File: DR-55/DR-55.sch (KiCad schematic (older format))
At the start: 0 parts

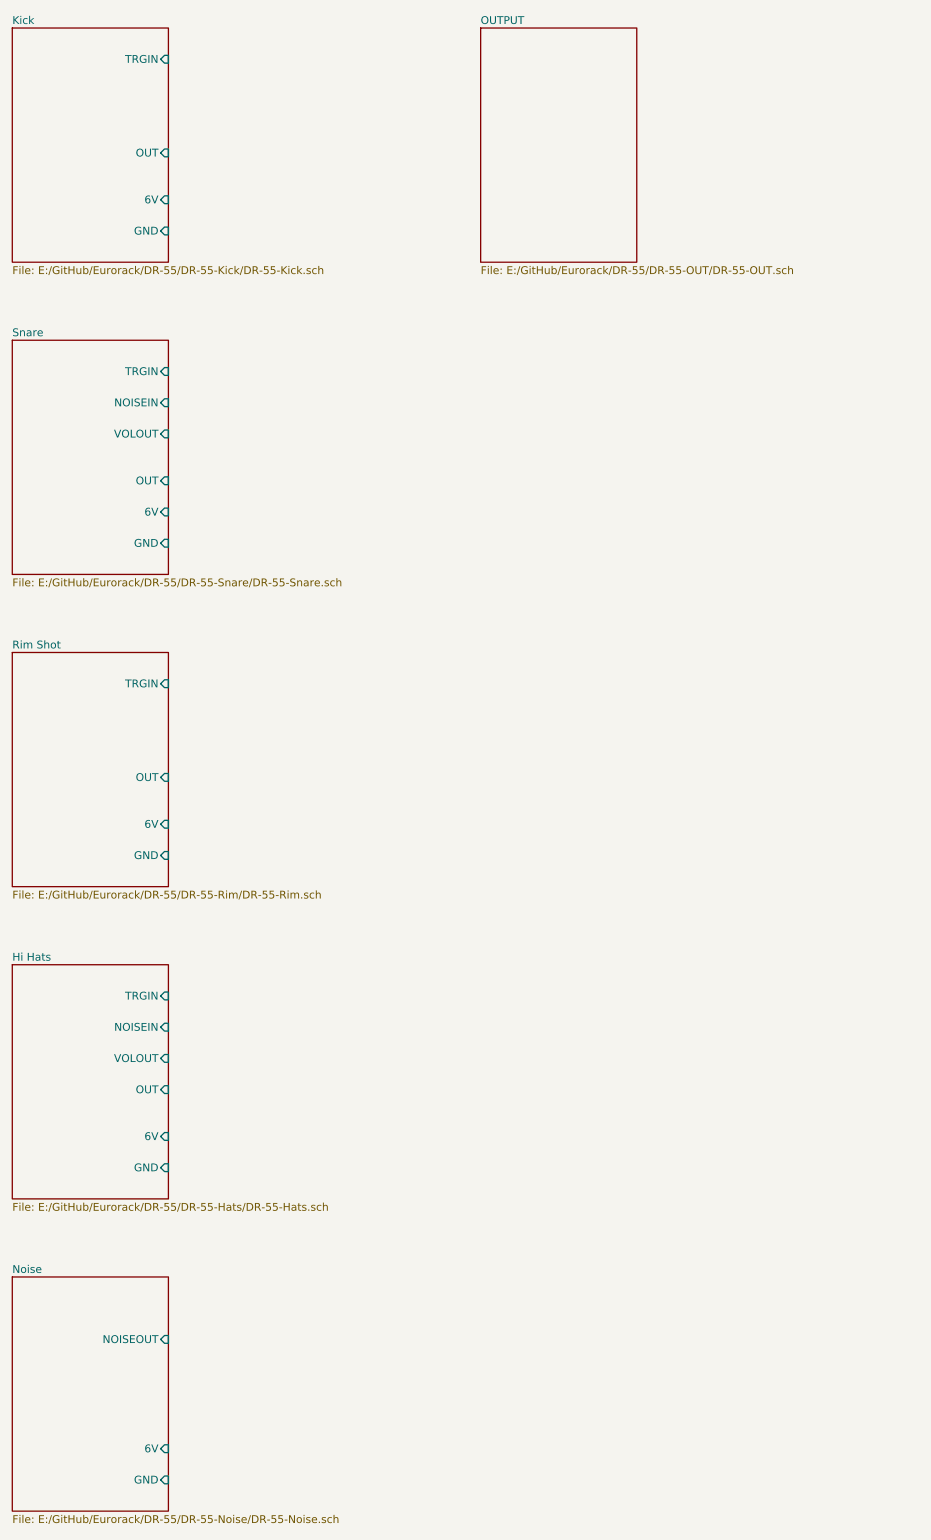
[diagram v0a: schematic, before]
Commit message: Output finished
Finished the output schematic and routed alll the traces between the submodules
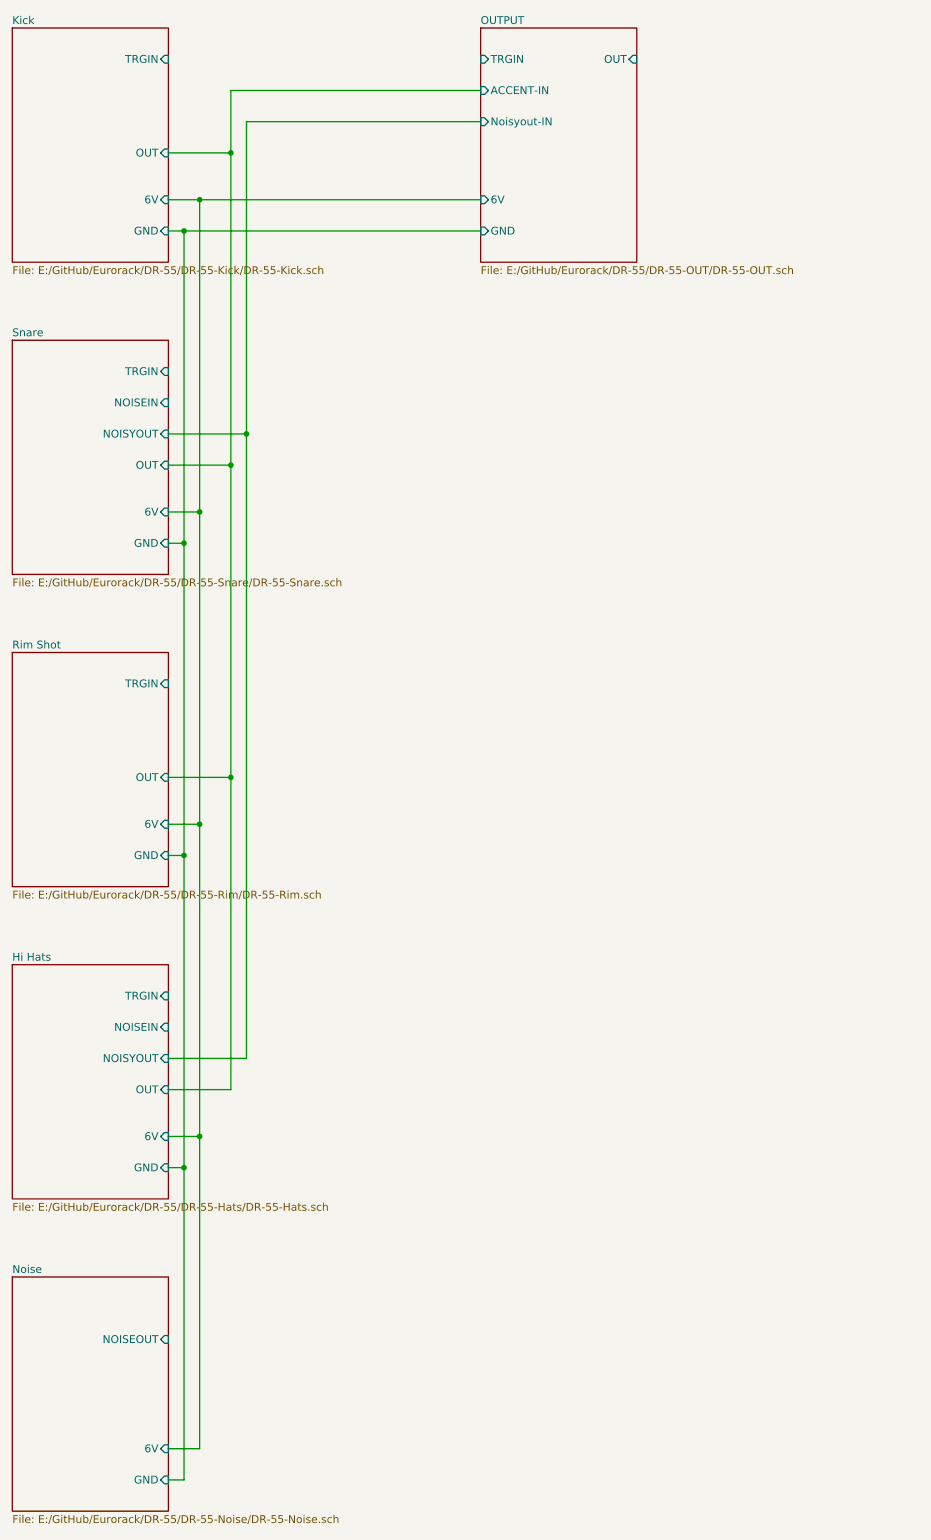
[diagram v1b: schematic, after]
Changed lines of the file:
@@
 F2 "TRGIN" I R 2000 3200 50
 F3 "GND" I R 2000 4300 50
-F4 "OUT" I R 2000 3900 50
+F4 "OUT" I R 2000 3800 50
 F5 "6V" I R 2000 4100 50
-F6 "VOLOUT" I R 2000 3600 50
-F7 "NOISEIN" I R 2000 3400 50
+F6 "NOISEIN" I R 2000 3400 50
+F7 "NOISYOUT" I R 2000 3600 50
 $EndSheet
 $Sheet
@@
 F4 "NOISEIN" I R 2000 7400 50
 F5 "OUT" I R 2000 7800 50
-F6 "VOLOUT" I R 2000 7600 50
-F7 "6V" I R 2000 8100 50
+F6 "6V" I R 2000 8100 50
+F7 "NOISYOUT" I R 2000 7600 50
 $EndSheet
 $Sheet
@@
 F0 "OUTPUT" 50
 F1 "E:/GitHub/Eurorack/DR-55/DR-55-OUT/DR-55-OUT.sch" 50
+F2 "TRGIN" I L 4000 1200 50
+F3 "GND" I L 4000 2300 50
+F4 "OUT" I R 5000 1200 50
+F5 "6V" I L 4000 2100 50
+F6 "ACCENT-IN" I L 4000 1400 50
+F7 "Noisyout-IN" I L 4000 1600 50
 $EndSheet
 $Sheet
@@
 F5 "GND" I R 2000 2300 50
 $EndSheet
+Wire Wire Line
+	4000 2100 2200 2100
+Wire Wire Line
+	4000 2300 2100 2300
+Wire Wire Line
+	2100 2300 2100 4300
+Wire Wire Line
+	2100 4300 2000 4300
+Connection ~ 2100 2300
+Wire Wire Line
+	2100 2300 2000 2300
+Wire Wire Line
+	2100 4300 2100 6300
+Wire Wire Line
+	2100 6300 2000 6300
+Connection ~ 2100 4300
+Wire Wire Line
+	2100 6300 2100 8300
+Wire Wire Line
+	2100 8300 2000 8300
+Connection ~ 2100 6300
+Wire Wire Line
+	2100 8300 2100 10300
+Wire Wire Line
+	2100 10300 2000 10300
+Connection ~ 2100 8300
+Connection ~ 2200 2100
+Wire Wire Line
+	2200 2100 2000 2100
+Wire Wire Line
+	2200 10100 2000 10100
+Wire Wire Line
+	2000 8100 2200 8100
+Connection ~ 2200 8100
+Wire Wire Line
+	2200 8100 2200 10100
+Wire Wire Line
+	2000 6100 2200 6100
+Connection ~ 2200 6100
+Wire Wire Line
+	2200 6100 2200 8100
+Wire Wire Line
+	2000 4100 2200 4100
+Connection ~ 2200 4100
+Wire Wire Line
+	2200 4100 2200 6100
+Wire Wire Line
+	2200 2100 2200 4100
+Wire Wire Line
+	2000 1800 2400 1800
+Wire Wire Line
+	2400 1800 2400 1400
+Wire Wire Line
+	2400 1400 4000 1400
+Wire Wire Line
+	2400 1800 2400 3800
+Wire Wire Line
+	2400 7800 2000 7800
+Connection ~ 2400 1800
+Wire Wire Line
+	2000 5800 2400 5800
+Connection ~ 2400 5800
+Wire Wire Line
+	2400 5800 2400 7800
+Wire Wire Line
+	2000 3800 2400 3800
+Connection ~ 2400 3800
+Wire Wire Line
+	2400 3800 2400 5800
+Wire Wire Line
+	4000 1600 2500 1600
+Wire Wire Line
+	2500 1600 2500 3600
+Wire Wire Line
+	2500 7600 2000 7600
+Wire Wire Line
+	2000 3600 2500 3600
+Connection ~ 2500 3600
+Wire Wire Line
+	2500 3600 2500 7600
 $EndSCHEMATC

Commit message: small changes
just some small overall changes (not relevant
)
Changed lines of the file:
@@
 $EndDescr
-$Sheet
-S 1000 3000 1000 1500
-U 62740CD0
-F0 "Snare" 50
-F1 "E:/GitHub/Eurorack/DR-55/DR-55-Snare/DR-55-Snare.sch" 50
-F2 "TRGIN" I R 2000 3200 50
-F3 "GND" I R 2000 4300 50
-F4 "OUT" I R 2000 3800 50
-F5 "6V" I R 2000 4100 50
-F6 "NOISEIN" I R 2000 3400 50
-F7 "NOISYOUT" I R 2000 3600 50
-$EndSheet
 $Sheet
 S 1000 7000 1000 1500
@@
 F5 "GND" I R 2000 2300 50
 $EndSheet
-Wire Wire Line
-	4000 2100 2200 2100
-Wire Wire Line
-	4000 2300 2100 2300
 Wire Wire Line
 	2100 2300 2100 4300
@@
 Wire Wire Line
 	2500 3600 2500 7600
+$Comp
+L power:+6V #PWR?
+U 1 1 62887F3E
+P 3900 2100
+AR Path="/6276643A/62887F3E" Ref="#PWR?"  Part="1"
+AR Path="/62740CD0/62887F3E" Ref="#PWR?"  Part="1"
+AR Path="/62804339/62887F3E" Ref="#PWR?"  Part="1"
+AR Path="/627A1DA3/62887F3E" Ref="#PWR?"  Part="1"
+AR Path="/62887F3E" Ref="#PWR?"  Part="1"
+F 0 "#PWR?" H 3900 1950 50  0001 C CNN
+F 1 "+6V" H 3915 2273 50  0000 C CNN
+F 2 "" H 3900 2100 50  0001 C CNN
+F 3 "" H 3900 2100 50  0001 C CNN
+	1    3900 2100
+	1    0    0    -1
+$EndComp
+$Comp
+L power:GND #PWR?
+U 1 1 6288900A
+P 3900 2300
+AR Path="/6276643A/6288900A" Ref="#PWR?"  Part="1"
+AR Path="/62740CD0/6288900A" Ref="#PWR?"  Part="1"
+AR Path="/62804339/6288900A" Ref="#PWR?"  Part="1"
+AR Path="/627A1DA3/6288900A" Ref="#PWR?"  Part="1"
+F 0 "#PWR?" H 3900 2050 50  0001 C CNN
+F 1 "GND" H 3905 2127 50  0000 C CNN
+F 2 "" H 3900 2300 50  0001 C CNN
+F 3 "" H 3900 2300 50  0001 C CNN
+	1    3900 2300
+	1    0    0    -1
+$EndComp
+Wire Wire Line
+	2100 2300 3900 2300
+Connection ~ 3900 2300
+Wire Wire Line
+	3900 2300 4000 2300
+Wire Wire Line
+	2200 2100 3900 2100
+Connection ~ 3900 2100
+Wire Wire Line
+	3900 2100 4000 2100
+$Sheet
+S 1000 3000 1000 1500
+U 62740CD0
+F0 "Snare" 50
+F1 "E:/GitHub/Eurorack/DR-55/DR-55-Snare/DR-55-Snare.sch" 50
+F2 "TRGIN" I R 2000 3200 50
+F3 "GND" I R 2000 4300 50
+F4 "OUT" I R 2000 3800 50
+F5 "6V" I R 2000 4100 50
+F6 "NOISEIN" I R 2000 3400 50
+F7 "NOISYOUT" I R 2000 3600 50
+$EndSheet
+Wire Wire Line
+	2000 3400 2700 3400
+Wire Wire Line
+	2700 3400 2700 7400
+Wire Wire Line
+	2700 7400 2000 7400
+Wire Wire Line
+	2700 7400 2700 9400
+Wire Wire Line
+	2700 9400 2000 9400
+Connection ~ 2700 7400
 $EndSCHEMATC

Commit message: Values
Added Values to all components
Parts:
- added J?: OUT, symbol Eurorack:Thonkiconn
- added J?: KICK, symbol Eurorack:Thonkiconn
- added J?: SNARE, symbol Eurorack:Thonkiconn
- added J?: RIM, symbol Eurorack:Thonkiconn
- added J?: HIHAT, symbol Eurorack:Thonkiconn
- added J?: ACCENT, symbol Eurorack:Thonkiconn
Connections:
- net GND: now also J?.3, J?.3, J?.3, J?.3, J?.3, J?.3
- net Hi Hats/TRGIN: now also J?.1
- net Kick/TRGIN: now also J?.1
- net OUTPUT/OUT: now also J?.1
- net OUTPUT/TRGIN: now also J?.1
- net Rim Shot/TRGIN: now also J?.1
- net Snare/TRGIN: now also J?.1
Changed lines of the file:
@@
-$EndSheet
-$Sheet
-S 4000 1000 1000 1500
-U 627A1DA3
-F0 "OUTPUT" 50
-F1 "E:/GitHub/Eurorack/DR-55/DR-55-OUT/DR-55-OUT.sch" 50
-F2 "TRGIN" I L 4000 1200 50
-F3 "GND" I L 4000 2300 50
-F4 "OUT" I R 5000 1200 50
-F5 "6V" I L 4000 2100 50
-F6 "ACCENT-IN" I L 4000 1400 50
-F7 "Noisyout-IN" I L 4000 1600 50
 $EndSheet
 $Sheet
@@
 AR Path="/62804339/6288900A" Ref="#PWR?"  Part="1"
 AR Path="/627A1DA3/6288900A" Ref="#PWR?"  Part="1"
+AR Path="/6288900A" Ref="#PWR?"  Part="1"
 F 0 "#PWR?" H 3900 2050 50  0001 C CNN
 F 1 "GND" H 3905 2127 50  0000 C CNN
@@
 $EndComp
 Wire Wire Line
-	2100 2300 3900 2300
+	2100 2300 3500 2300
 Connection ~ 3900 2300
 Wire Wire Line
@@
 	2700 9400 2000 9400
 Connection ~ 2700 7400
+$Comp
+L Eurorack:Thonkiconn J?
+U 1 1 627AD8C4
+P 5750 1200
+F 0 "J?" H 5794 1168 50  0000 L CNN
+F 1 "OUT" H 5794 1077 50  0000 L CNN
+F 2 "" H 5650 1250 50  0001 C CNN
+F 3 "" H 5650 1250 50  0001 C CNN
+	1    5750 1200
+	1    0    0    -1
+$EndComp
+$Sheet
+S 4000 1000 1000 1500
+U 627A1DA3
+F0 "OUTPUT" 50
+F1 "E:/GitHub/Eurorack/DR-55/DR-55-OUT/DR-55-OUT.sch" 50
+F2 "TRGIN" I L 4000 1200 50
+F3 "GND" I L 4000 2300 50
+F4 "OUT" I R 5000 1200 50
+F5 "6V" I L 4000 2100 50
+F6 "ACCENT-IN" I L 4000 1400 50
+F7 "Noisyout-IN" I L 4000 1600 50
+$EndSheet
+Wire Wire Line
+	5000 1200 5500 1200
+$Comp
+L power:GND #PWR?
+U 1 1 627B2033
+P 5750 1500
+AR Path="/6276643A/627B2033" Ref="#PWR?"  Part="1"
+AR Path="/62740CD0/627B2033" Ref="#PWR?"  Part="1"
+AR Path="/62804339/627B2033" Ref="#PWR?"  Part="1"
+AR Path="/627A1DA3/627B2033" Ref="#PWR?"  Part="1"
+AR Path="/627B2033" Ref="#PWR?"  Part="1"
+F 0 "#PWR?" H 5750 1250 50  0001 C CNN
+F 1 "GND" H 5755 1327 50  0000 C CNN
+F 2 "" H 5750 1500 50  0001 C CNN
+F 3 "" H 5750 1500 50  0001 C CNN
+	1    5750 1500
+	1    0    0    -1
+$EndComp
+Wire Wire Line
+	5750 1500 5750 1400
+$Comp
+L Eurorack:Thonkiconn J?
+U 1 1 627B3297
+P 4250 3000
+F 0 "J?" H 4294 2968 50  0000 L CNN
+F 1 "KICK" H 4294 2877 50  0000 L CNN
+F 2 "" H 4150 3050 50  0001 C CNN
+F 3 "" H 4150 3050 50  0001 C CNN
+	1    4250 3000
+	1    0    0    -1
+$EndComp
+$Comp
+L Eurorack:Thonkiconn J?
+U 1 1 627B659A
+P 4250 3500
+F 0 "J?" H 4294 3468 50  0000 L CNN
+F 1 "SNARE" H 4294 3377 50  0000 L CNN
+F 2 "" H 4150 3550 50  0001 C CNN
+F 3 "" H 4150 3550 50  0001 C CNN
+	1    4250 3500
+	1    0    0    -1
+$EndComp
+$Comp
+L Eurorack:Thonkiconn J?
+U 1 1 627B6F00
+P 4250 4000
+F 0 "J?" H 4294 3968 50  0000 L CNN
+F 1 "RIM" H 4294 3877 50  0000 L CNN
+F 2 "" H 4150 4050 50  0001 C CNN
+F 3 "" H 4150 4050 50  0001 C CNN
+	1    4250 4000
+	1    0    0    -1
+$EndComp
+$Comp
+L Eurorack:Thonkiconn J?
+U 1 1 627B7907
+P 4250 4500
+F 0 "J?" H 4294 4468 50  0000 L CNN
+F 1 "HIHAT" H 4294 4377 50  0000 L CNN
+F 2 "" H 4150 4550 50  0001 C CNN
+F 3 "" H 4150 4550 50  0001 C CNN
+	1    4250 4500
+	1    0    0    -1
+$EndComp
+$Comp
+L Eurorack:Thonkiconn J?
+U 1 1 627B86EE
+P 4250 5000
+F 0 "J?" H 4294 4968 50  0000 L CNN
+F 1 "ACCENT" H 4294 4877 50  0000 L CNN
+F 2 "" H 4150 5050 50  0001 C CNN
+F 3 "" H 4150 5050 50  0001 C CNN
+	1    4250 5000
+	1    0    0    -1
+$EndComp
+Wire Wire Line
+	4250 3200 3500 3200
+Wire Wire Line
+	3500 3200 3500 3700
+Wire Wire Line
+	3500 5200 4250 5200
+Wire Wire Line
+	4250 4700 3500 4700
+Connection ~ 3500 4700
+Wire Wire Line
+	3500 4700 3500 5200
+Wire Wire Line
+	3500 4200 4250 4200
+Connection ~ 3500 4200
+Wire Wire Line
+	3500 4200 3500 4700
+Wire Wire Line
+	4250 3700 3500 3700
+Connection ~ 3500 3700
+Wire Wire Line
+	3500 3700 3500 4200
+Wire Wire Line
+	3500 3200 3500 2300
+Connection ~ 3500 3200
+Connection ~ 3500 2300
+Wire Wire Line
+	3500 2300 3900 2300
+Wire Wire Line
+	4000 3000 2700 3000
+Wire Wire Line
+	2700 3000 2700 1200
+Wire Wire Line
+	4000 3500 2800 3500
+Wire Wire Line
+	2800 3500 2800 3200
+Wire Wire Line
+	2800 3200 2000 3200
+Wire Wire Line
+	4000 4000 2900 4000
+Wire Wire Line
+	2900 4000 2900 5200
+Wire Wire Line
+	2900 5200 2000 5200
+Wire Wire Line
+	4000 4500 3000 4500
+Wire Wire Line
+	3000 4500 3000 7200
+Wire Wire Line
+	3000 7200 2000 7200
+Wire Wire Line
+	4000 5000 3100 5000
+Wire Wire Line
+	3100 5000 3100 1200
+Wire Wire Line
+	3100 1200 4000 1200
+Wire Wire Line
+	2700 1200 2000 1200
 $EndSCHEMATC

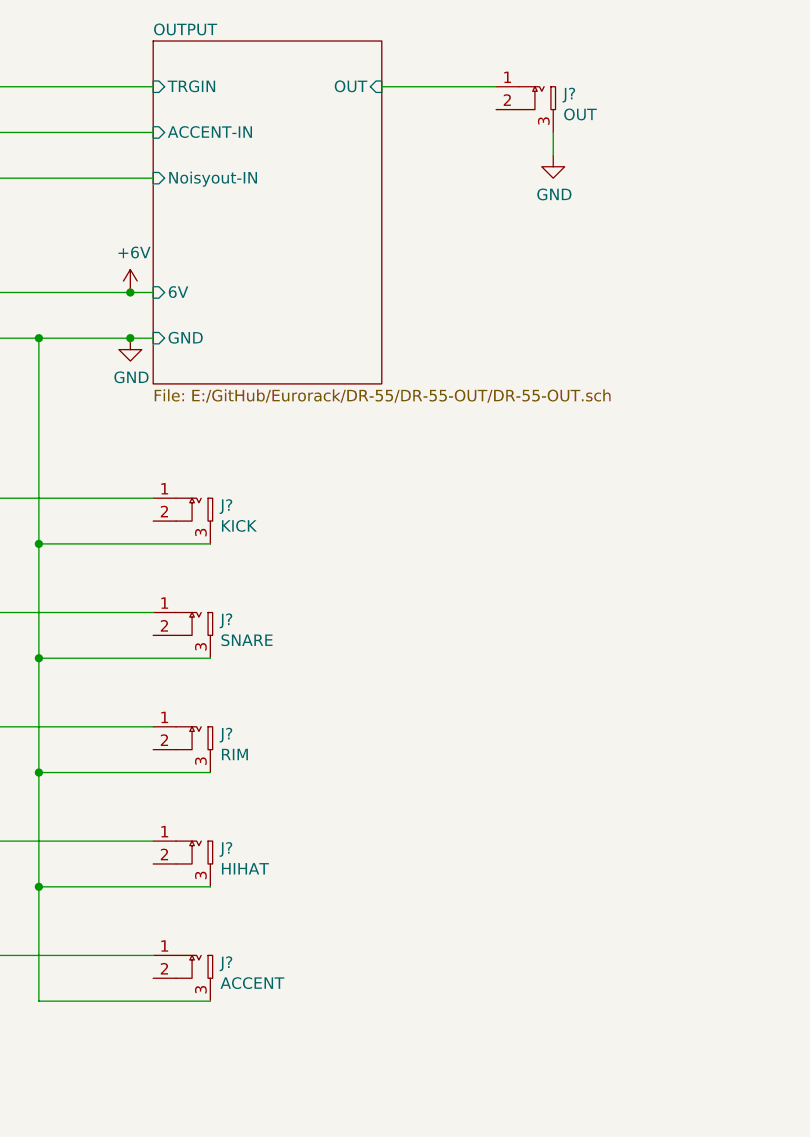
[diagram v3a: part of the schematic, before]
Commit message: Footprints added
Added most of the footprints for a 0805 SMD PCB. some placeholder footprints added and some missing
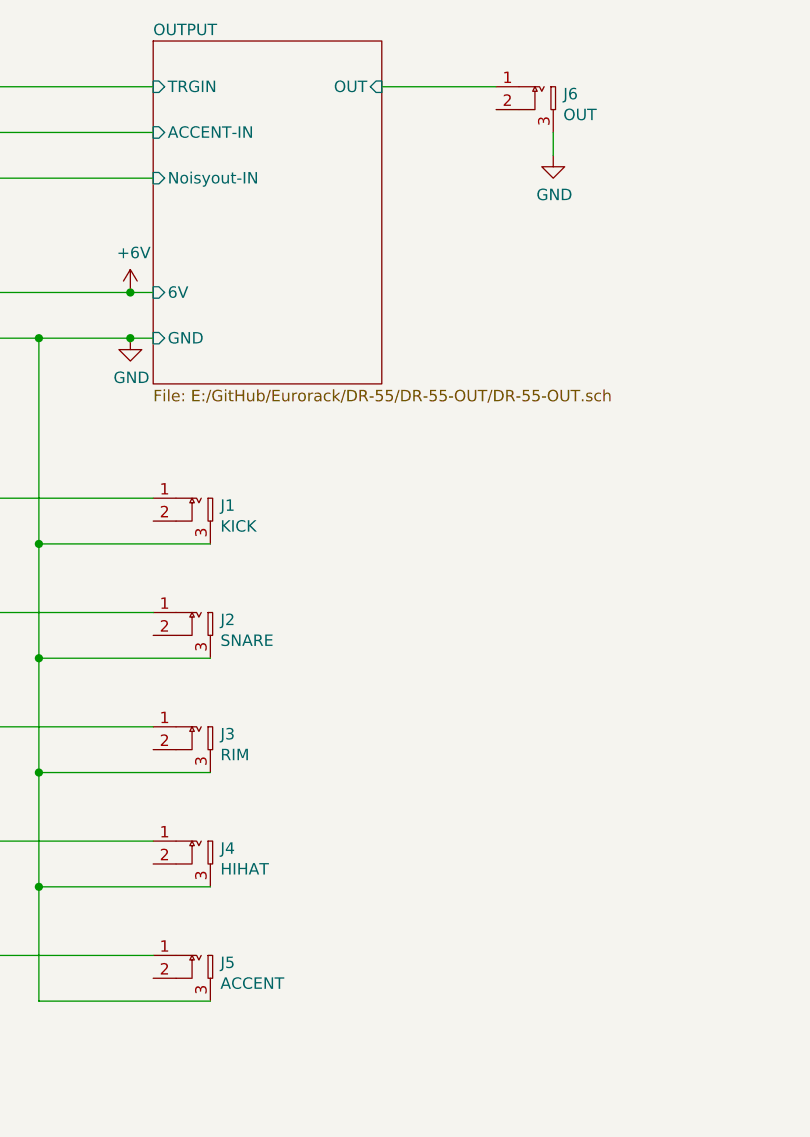
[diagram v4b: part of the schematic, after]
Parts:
- J1, J2, J3, J4, J5, J6: renamed from J?; footprint (none) -> Connector_PinHeader_2.54mm:PinHeader_1x03_P2.54mm_Vertical
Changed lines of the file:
@@
 AR Path="/62804339/62887F3E" Ref="#PWR?"  Part="1"
 AR Path="/627A1DA3/62887F3E" Ref="#PWR?"  Part="1"
-AR Path="/62887F3E" Ref="#PWR?"  Part="1"
-F 0 "#PWR?" H 3900 1950 50  0001 C CNN
+AR Path="/62887F3E" Ref="#PWR0101"  Part="1"
+F 0 "#PWR0101" H 3900 1950 50  0001 C CNN
 F 1 "+6V" H 3915 2273 50  0000 C CNN
 F 2 "" H 3900 2100 50  0001 C CNN
@@
 AR Path="/62804339/6288900A" Ref="#PWR?"  Part="1"
 AR Path="/627A1DA3/6288900A" Ref="#PWR?"  Part="1"
-AR Path="/6288900A" Ref="#PWR?"  Part="1"
-F 0 "#PWR?" H 3900 2050 50  0001 C CNN
+AR Path="/6288900A" Ref="#PWR0102"  Part="1"
+F 0 "#PWR0102" H 3900 2050 50  0001 C CNN
 F 1 "GND" H 3905 2127 50  0000 C CNN
 F 2 "" H 3900 2300 50  0001 C CNN
@@
 Connection ~ 2700 7400
 $Comp
-L Eurorack:Thonkiconn J?
+L Eurorack:Thonkiconn J6
 U 1 1 627AD8C4
 P 5750 1200
-F 0 "J?" H 5794 1168 50  0000 L CNN
+F 0 "J6" H 5794 1168 50  0000 L CNN
 F 1 "OUT" H 5794 1077 50  0000 L CNN
-F 2 "" H 5650 1250 50  0001 C CNN
+F 2 "Connector_PinHeader_2.54mm:PinHeader_1x03_P2.54mm_Vertical" H 5650 1250 50  0001 C CNN
 F 3 "" H 5650 1250 50  0001 C CNN
 	1    5750 1200
@@
 AR Path="/62804339/627B2033" Ref="#PWR?"  Part="1"
 AR Path="/627A1DA3/627B2033" Ref="#PWR?"  Part="1"
-AR Path="/627B2033" Ref="#PWR?"  Part="1"
-F 0 "#PWR?" H 5750 1250 50  0001 C CNN
+AR Path="/627B2033" Ref="#PWR0103"  Part="1"
+F 0 "#PWR0103" H 5750 1250 50  0001 C CNN
 F 1 "GND" H 5755 1327 50  0000 C CNN
 F 2 "" H 5750 1500 50  0001 C CNN
@@
 	5750 1500 5750 1400
 $Comp
-L Eurorack:Thonkiconn J?
+L Eurorack:Thonkiconn J1
 U 1 1 627B3297
 P 4250 3000
-F 0 "J?" H 4294 2968 50  0000 L CNN
+F 0 "J1" H 4294 2968 50  0000 L CNN
 F 1 "KICK" H 4294 2877 50  0000 L CNN
-F 2 "" H 4150 3050 50  0001 C CNN
+F 2 "Connector_PinHeader_2.54mm:PinHeader_1x03_P2.54mm_Vertical" H 4150 3050 50  0001 C CNN
 F 3 "" H 4150 3050 50  0001 C CNN
 	1    4250 3000
@@
 $EndComp
 $Comp
-L Eurorack:Thonkiconn J?
+L Eurorack:Thonkiconn J2
 U 1 1 627B659A
 P 4250 3500
-F 0 "J?" H 4294 3468 50  0000 L CNN
+F 0 "J2" H 4294 3468 50  0000 L CNN
 F 1 "SNARE" H 4294 3377 50  0000 L CNN
-F 2 "" H 4150 3550 50  0001 C CNN
+F 2 "Connector_PinHeader_2.54mm:PinHeader_1x03_P2.54mm_Vertical" H 4150 3550 50  0001 C CNN
 F 3 "" H 4150 3550 50  0001 C CNN
 	1    4250 3500
@@
 $EndComp
 $Comp
-L Eurorack:Thonkiconn J?
+L Eurorack:Thonkiconn J3
 U 1 1 627B6F00
 P 4250 4000
-F 0 "J?" H 4294 3968 50  0000 L CNN
+F 0 "J3" H 4294 3968 50  0000 L CNN
 F 1 "RIM" H 4294 3877 50  0000 L CNN
-F 2 "" H 4150 4050 50  0001 C CNN
+F 2 "Connector_PinHeader_2.54mm:PinHeader_1x03_P2.54mm_Vertical" H 4150 4050 50  0001 C CNN
 F 3 "" H 4150 4050 50  0001 C CNN
 	1    4250 4000
@@
 $EndComp
 $Comp
-L Eurorack:Thonkiconn J?
+L Eurorack:Thonkiconn J4
 U 1 1 627B7907
 P 4250 4500
-F 0 "J?" H 4294 4468 50  0000 L CNN
+F 0 "J4" H 4294 4468 50  0000 L CNN
 F 1 "HIHAT" H 4294 4377 50  0000 L CNN
-F 2 "" H 4150 4550 50  0001 C CNN
+F 2 "Connector_PinHeader_2.54mm:PinHeader_1x03_P2.54mm_Vertical" H 4150 4550 50  0001 C CNN
 F 3 "" H 4150 4550 50  0001 C CNN
 	1    4250 4500
@@
 $EndComp
 $Comp
-L Eurorack:Thonkiconn J?
+L Eurorack:Thonkiconn J5
 U 1 1 627B86EE
 P 4250 5000
-F 0 "J?" H 4294 4968 50  0000 L CNN
+F 0 "J5" H 4294 4968 50  0000 L CNN
 F 1 "ACCENT" H 4294 4877 50  0000 L CNN
-F 2 "" H 4150 5050 50  0001 C CNN
+F 2 "Connector_PinHeader_2.54mm:PinHeader_1x03_P2.54mm_Vertical" H 4150 5050 50  0001 C CNN
 F 3 "" H 4150 5050 50  0001 C CNN
 	1    4250 5000
